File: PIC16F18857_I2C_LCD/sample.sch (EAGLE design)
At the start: 18 parts, among them CN1 12V_IN, CN2 PIC_CN_H, SW1 10-XX, U1 XC6202P332TH, U2 PIC16F18857-I/SP, U3 AE-AQM1602A, U4 STTS751-0WB3F

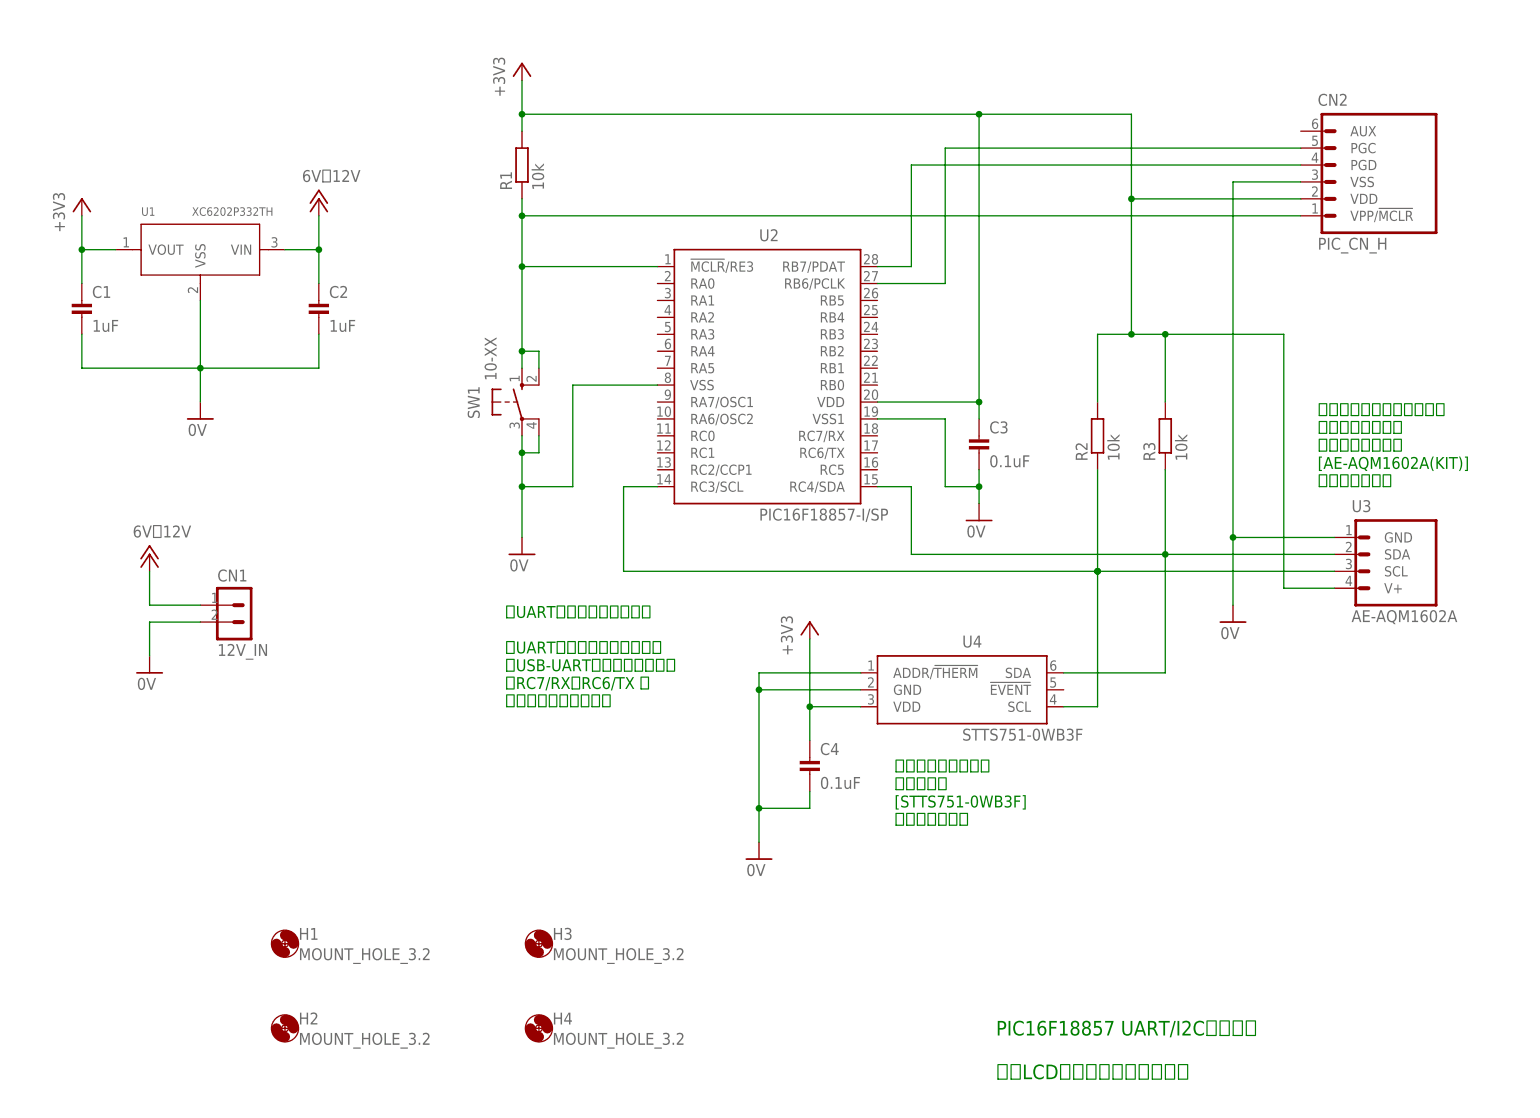
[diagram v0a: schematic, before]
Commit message: RTCCを接続した回路図を作成
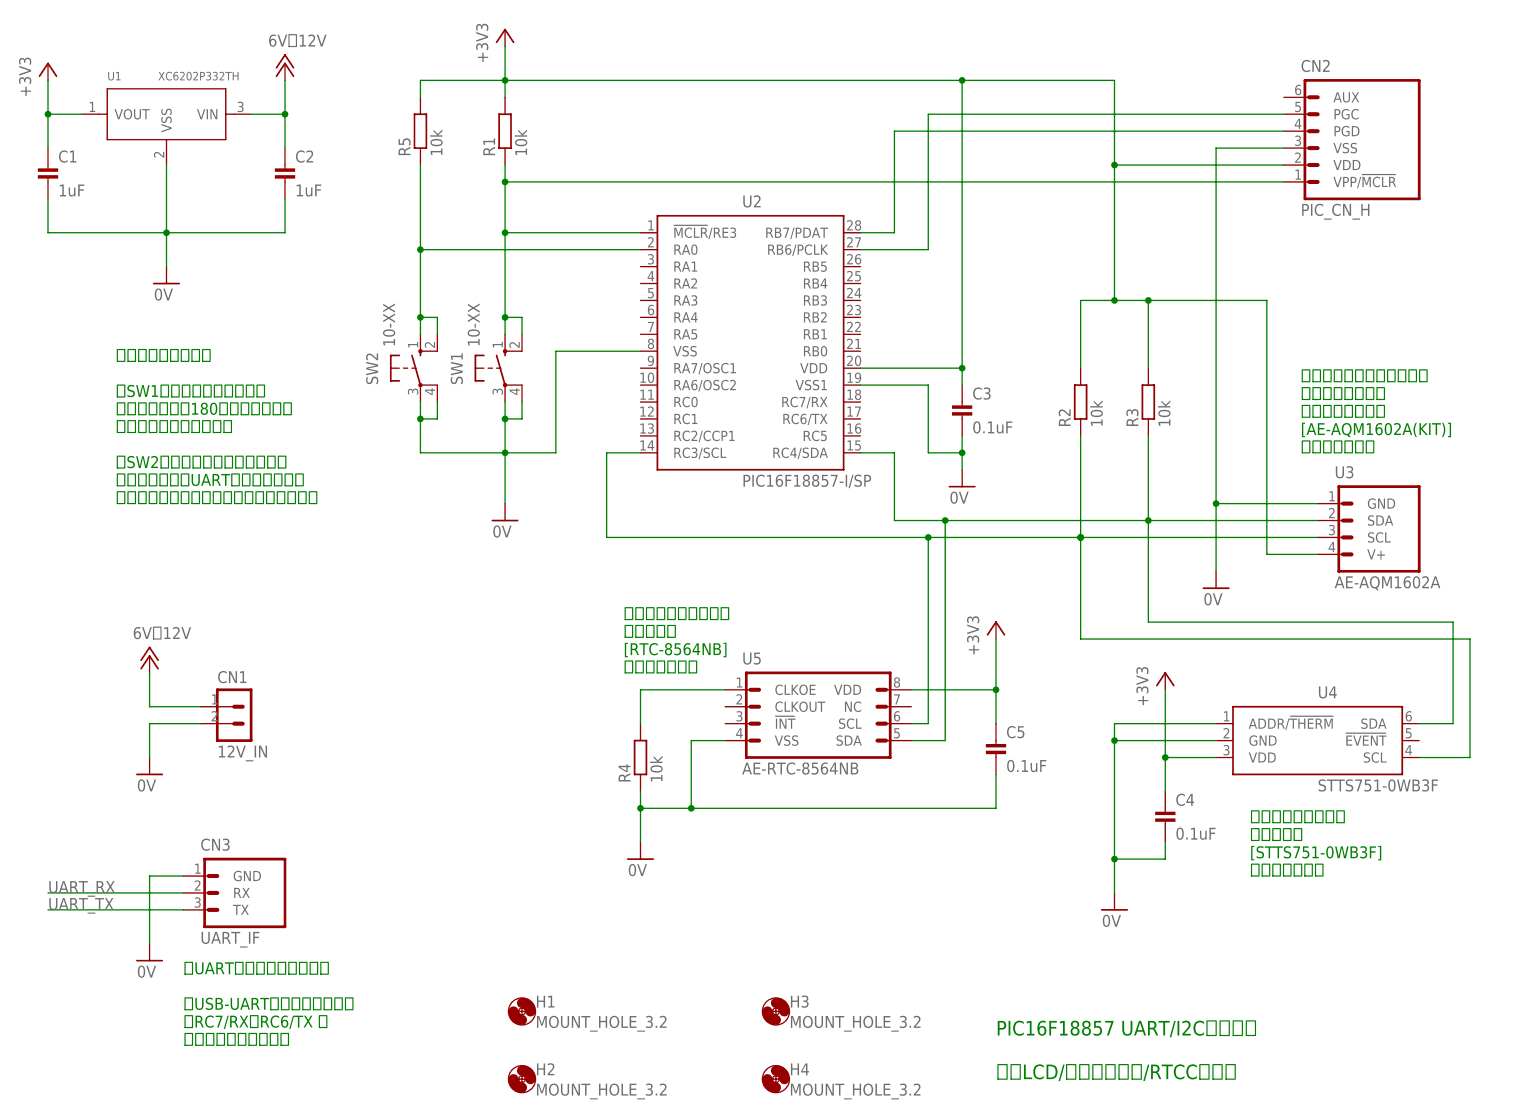
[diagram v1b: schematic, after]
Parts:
- added C5: 0.1uF, Parts:CAP_200MIL
- added CN3: UART_IF, PartsForProto:UART_IF
- added R4, R5: 10k, Parts:RESISTOR_300MIL
- added SW2: 10-XX, Parts:10-XX
- added U5: AE-RTC-8564NB, PartsForProto:AE-RTC-8564NB
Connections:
- new net N$8: R4.2, U5.CLKOE
- new net N$9: R5.1, SW2.S, SW2.S1, U2.RA0
- new net UART_RX: CN3.RX
- new net UART_TX: CN3.TX
- net +3V3: now also C5.1, R5.2, U5.VDD
- net 0V: now also C5.2, CN3.GND, R4.1, SW2.P, SW2.P1, U5.VSS
- net N$1: now also U5.SDA
- net N$6: now also U5.SCL
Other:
- note added: "PIC16F18857 UART/I2Cサンプル 小型LCD/温度センサー/RTCCを接続"
- note added: "【UARTのご使用について】 USB-UART変換基板などを、 RC7/RX、RC6/TX に 接続してください。"
- note added: "【タクトスイッチ】 SW1：カウントダウン開始 ボタン押下で180秒間のカウント ダウンが開始されます SW2：時刻アジャスト入力開始 ボタン押下でUARTにアジャスト用 文字列の入力プロンプトが表示されます"
- note added: "リアルタイムクロック モジュール [RTC-8564NB] を使用します。"
- note removed: "PIC16F18857 UART/I2Cサンプル 小型LCDと温度センサーを接続"
- note removed: "【UARTのご使用について】 UART出力させたい場合は、 USB-UART変換基板などを、 RC7/RX、RC6/TX に 接続してください。"
- moved on the sheet: C1, C2, C3, C4, CN1, CN2, H1, H2, H3, H4, R1, R2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

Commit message: RTCCに常時給電させるように回路を修正
同時に部品番号／コメントを見直し
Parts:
- added C6: 0.1uF, Parts:CAP_200MIL
- added G1: CR2032H, Parts:CR2032H
- C3: value 0.1uF -> 10uF; device Parts:CAP_200MIL -> Parts:ELECAP_200MIL
- CN2: value PIC_CN_H -> UART_IF; device Connectors:PIC_CN_H -> PartsForProto:UART_IF
- CN3: value UART_IF -> PIC_CN_H; device PartsForProto:UART_IF -> Connectors:PIC_CN_H
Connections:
- new net +3V: C6.1, G1.+, U5.VDD
- net +12V: now also C3.+
- net +3V3: now also CN3.VDD, R4.2; no longer C3.1, CN2.VDD, R5.2, U5.VDD
- net 0V: now also C3.-, C6.2, CN2.GND, CN3.VSS, G1.-, R5.1; no longer C3.2, CN2.VSS, CN3.GND, R4.1
- net N$1: now also R4.1; no longer R3.1
- net N$2: now also CN3.PGD; no longer CN2.PGD
- net N$3: now also R2.1, SW2.S, SW2.S1, U2.RA0; no longer CN2.VPP/!MCLR, R1.1, SW1.S, SW1.S1, U2.!MCLR!/RE3
- net N$4: now also CN3.PGC; no longer CN2.PGC
- net N$6: now also R3.1; no longer R2.1
- net N$8: now also R5.2; no longer R4.2
- net N$9: now also CN3.VPP/!MCLR, R1.1, SW1.S, SW1.S1, U2.!MCLR!/RE3; no longer R5.1, SW2.S, SW2.S1, U2.RA0
- net UART_RX: now also CN2.RX, U2.RC7/RX; no longer CN3.RX
- net UART_TX: now also CN2.TX, U2.RC6/TX; no longer CN3.TX
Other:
- note added: "PIC16F18857 UART/I2Cサンプル 小型LCD／温度センサー／ RTCCを接続"
- note added: "【CR2032(ボタン乾電池)】 リアルタイムクロック モジュールには、常時 3Vを給電してください。 CR2032から非給電時に マイコンを起動しても、 リアルタイムクロックは 動作しませんので ご注意ください。"
- note removed: "PIC16F18857 UART/I2Cサンプル 小型LCD/温度センサー/RTCCを接続"
- moved on the sheet: C4, C5, CN1, R1, R2, R3, R4, R5, SW1, SW2

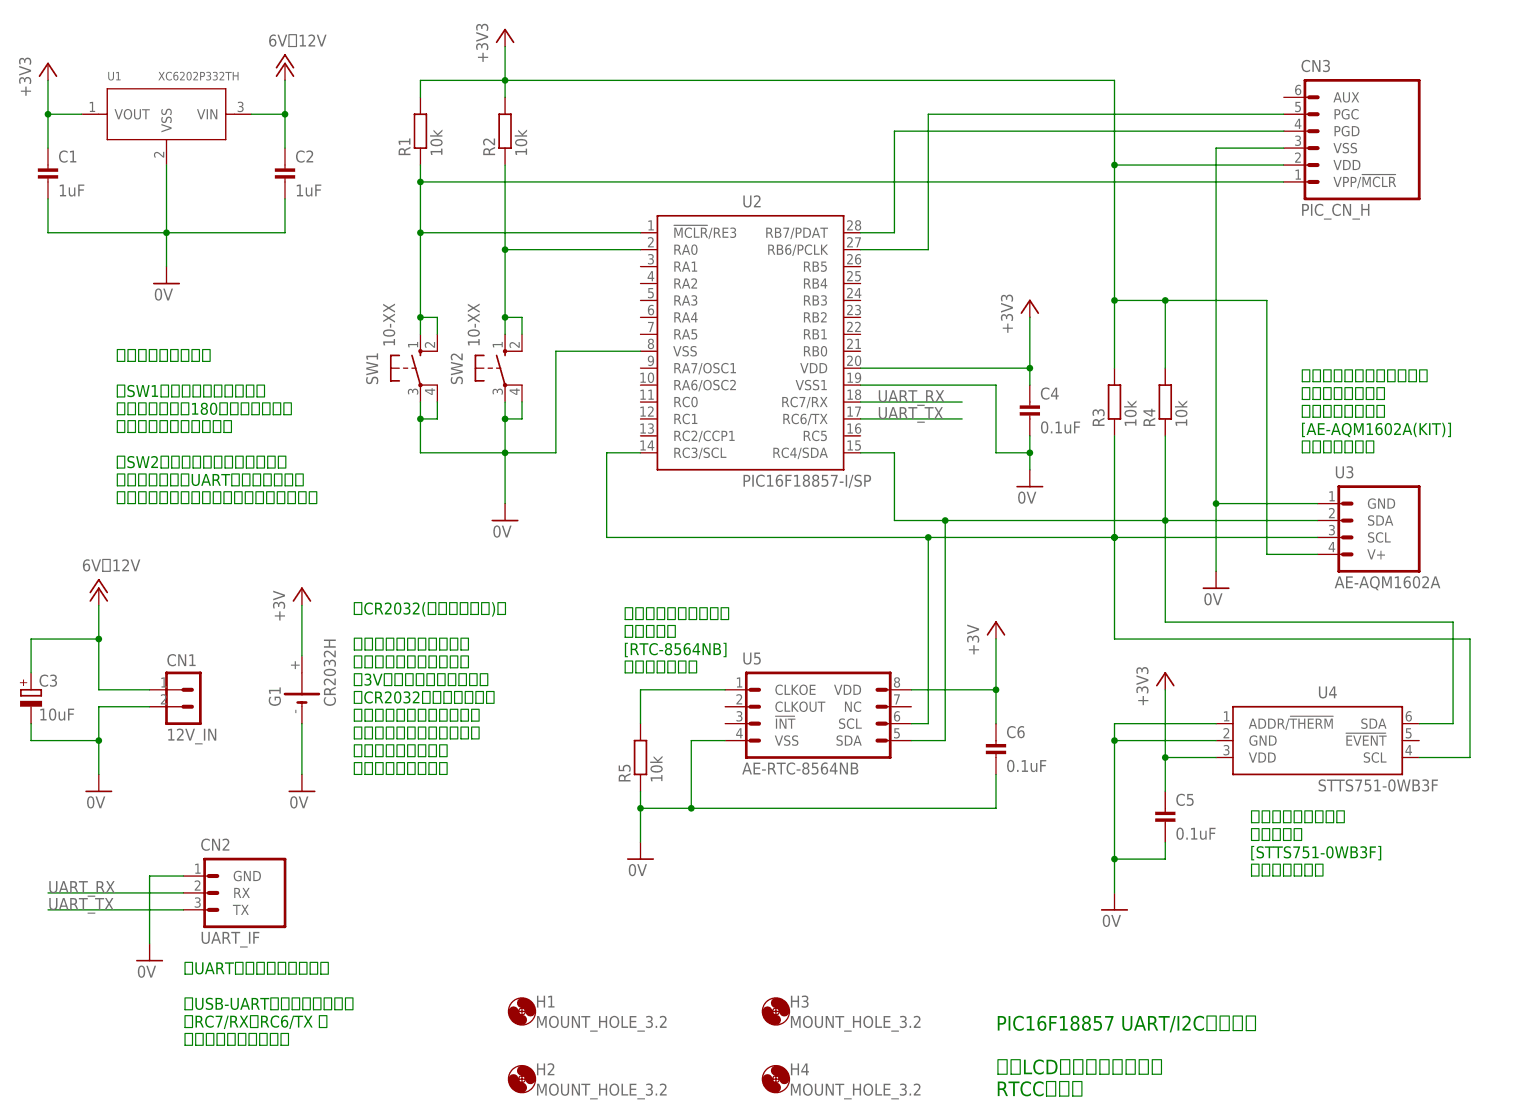
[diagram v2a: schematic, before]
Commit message: 回路から使用しないスイッチを削除
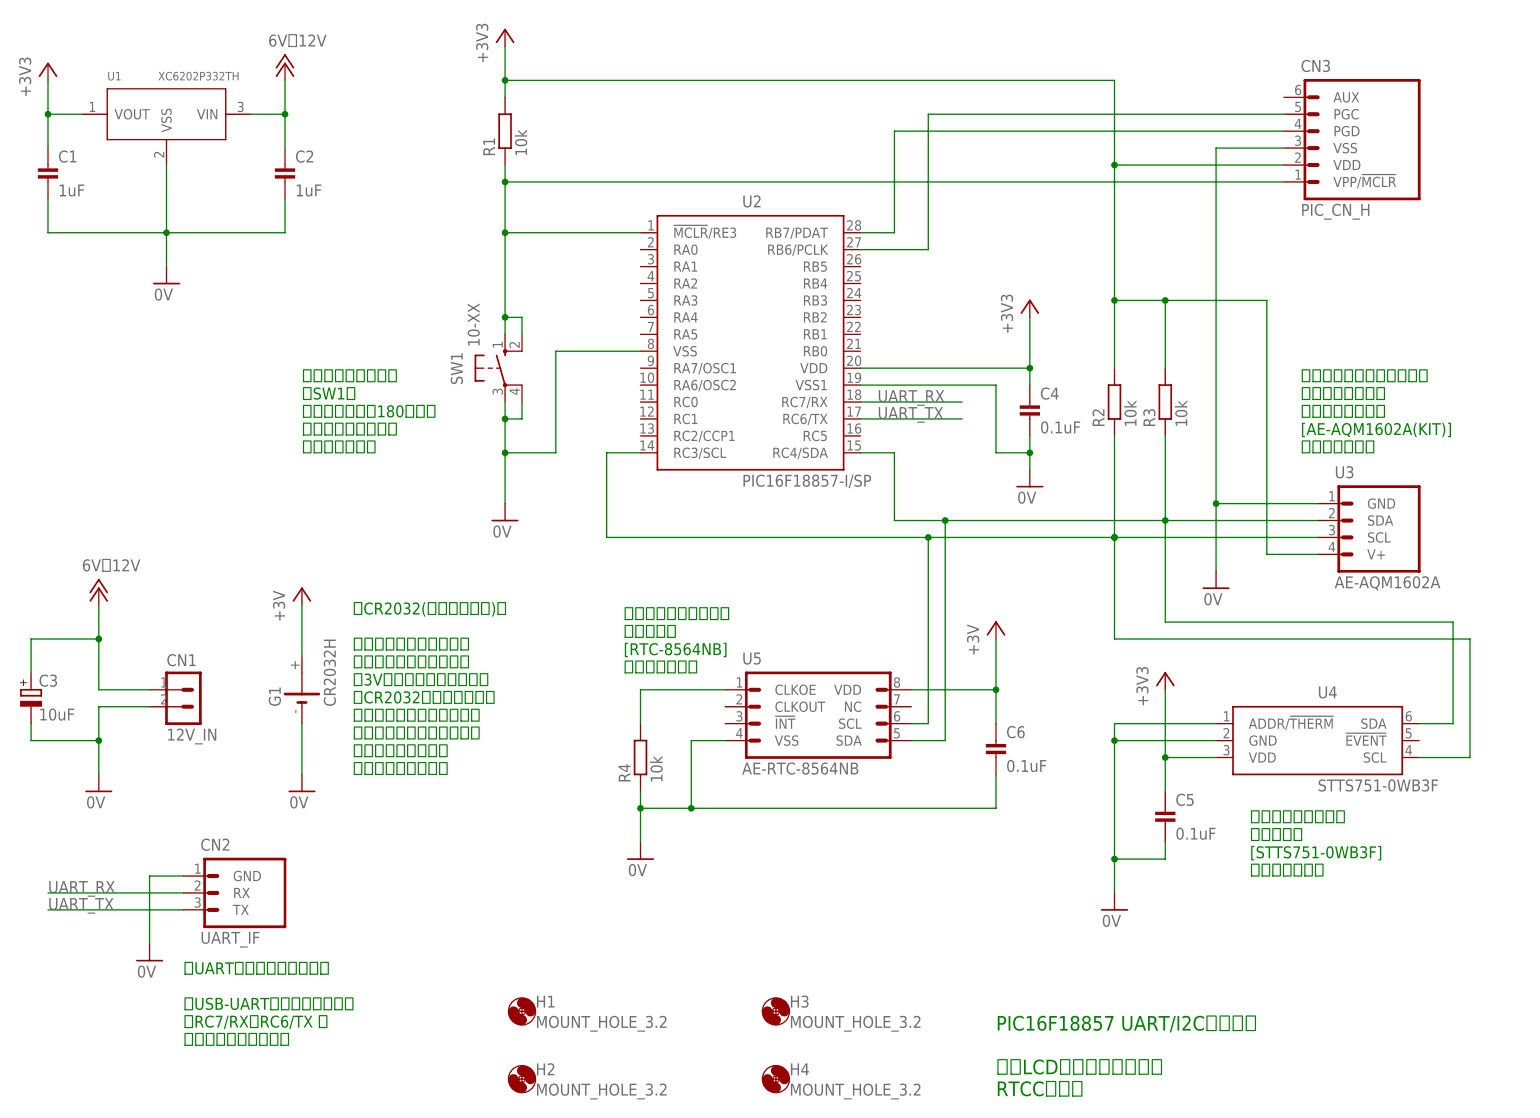
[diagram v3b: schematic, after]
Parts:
- removed R5: 10k, Parts:RESISTOR_300MIL
- removed SW2: 10-XX, Parts:10-XX
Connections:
- removed net N$3: R2.1, SW2.S, SW2.S1, U2.RA0
- net +3V3: no longer R4.2
- net 0V: now also R4.1; no longer R5.1, SW2.P, SW2.P1
- net N$1: now also R3.1; no longer R4.1
- net N$6: now also R2.1; no longer R3.1
- net N$8: now also R4.2; no longer R5.2
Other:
- note added: "【タクトスイッチ】 SW1： ボタン押下で180秒間の カウントダウンが 開始されます"
- note removed: "【タクトスイッチ】 SW1：カウントダウン開始 ボタン押下で180秒間のカウント ダウンが開始されます SW2：時刻アジャスト入力開始 ボタン押下でUARTにアジャスト用 文字列の入力プロンプトが表示されます"
- moved on the sheet: R1, R2, R3, R4, SW1
